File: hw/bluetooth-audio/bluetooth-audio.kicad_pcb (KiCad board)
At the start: 4 copper layers, 32.4 x 55.2 mm, 100 parts, among them J1 AudioJack4_Ground, J2 USB_C_Receptacle_USB2.0, J3 Conn_01x06, J4 2x5 JTAG header, Q1 UMH3N, U1 ESP32D0WD-V3, U2 CH340K, U3 TLV71318PDBV, U4 ES8388, U5 USBLC6-2SC6, U6 W25Q32JVZP, U7 NCP1117-3.3_SOT223, Y1 Crystal 40 MHz 10pF

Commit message: Rev B micro sheet: correctness fixes, CH340 load switch, full ESP32 GPIO map
Micro-sheet fixes (netlist-verified):
- UART TX/RX crossover corrected (U0RXD<->CH340 TXD, U0TXD<->CH340 RXD)
- Flash IO2/IO3 uncrossed (GPIO9/SPIWP->IO2, GPIO10/SPIHD->IO3)
- Digital rail unified to +3V3_SYS; EN pull-up (R11) reconnected

CH340K high-side load switch (delta #16):
- Q2 AO3401A (SOT-23, LCSC C15127) + R40 100k gate pull-down = default-ON
  so the ROM bootloader is powered for USB flashing; gate CH340_EN on GPIO21,
  firmware drives high to disable the bridge on battery

Full ESP32 interface wired (see design-overview.md 3.8):
- EN1->16, EN2->17, AUDIO_VCC_EN->4, AUDIO_SW->5, CH340_EN->21, CHARGE_EN->2
- /PGOOD->38, /CHG->32; ADC1 senses BAT_ADC->34, USB_CC1->36, USB_CC2->37,
  USB_VBUS_SENSE->39; GPIO33 spare
- AUDIO_SW drives both TS5A23159 inputs (LOW=RX, HIGH=TX); pinout verified
  against TI datasheet (COM=jack, NC=codec-out, NO=codec-in, both channels)

Docs:
- design-overview.md: committed GPIO map with strapping-pin FW/HW implications
  (3.8), AUDIO_SW/CHARGE_EN firmware notes (9), updated status (10)
- design-review-micro.md: micro-sheet systems review
- added WCH CH340 datasheet; updated TODO
- gitignore MCP snapshot/log artifacts

Co-Authored-By: Claude Opus 4.8 <noreply@anthropic.com>
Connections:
- C19 pad 1: +3V3 -> CH340_VCC
- U1 pad 42: unconnected-(U1-GPIO21-Pad42) -> CH340_EN

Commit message: Audio sheet redesign: ZTS6216 mic, PJ-3537S jack, shared 47 uF coupling
Rework the audio subsystem and record the rationale.

- Microphone: switch to ZillTek ZTS6216 (self-biased single-ended, C0G
  mic coupling C41/C42 per datasheet); pseudo-diff RIN1 provisioned DNP.
- Jack: PJ-3537S 3-pole TRS + detect switch (custom symbol + footprint).
- Coupling: single shared 47 uF electrolytic pair (C1/C21) on the jack
  side of the TX/RX switch, serving both RX and TX; R22/R23 bleed.
- TX input: BAT54S series-Schottky clamps (D7/D8) to AVDD/GND,
  line-level-only, PGA 0 dB.
- Ground loop: battery-only playback is the plan of record (no
  transformer footprint).
- Add TS5A23159 switch, ZTS6216 and PJ-3537S datasheets.
- Add systems design review (docs/design-review-audio.md) and update
  design overview with coupling-cap sizing.
- PCB layout updated to match.

Co-Authored-By: Claude Opus 4.8 <noreply@anthropic.com>
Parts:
- added C2: 1uF, Capacitor_SMD:C_1206_3216Metric, F.Cu at (188.8, 94.2)
- added C20: 1uF, Capacitor_SMD:C_0603_1608Metric, F.Cu at (207.5, 119.2)
- added C23: 1uF, Capacitor_SMD:C_0402_1005Metric, F.Cu at (218.6, 104.5)
- added C25: 1uF, Capacitor_SMD:C_0402_1005Metric, F.Cu at (218.6, 106.5)
- added C45: 10nF, Capacitor_SMD:C_0402_1005Metric, F.Cu at (218.6, 116.8)
- added C46: 100nF, Capacitor_SMD:C_0402_1005Metric, F.Cu at (218.6, 108.4)
- added C47: 10uF, Capacitor_SMD:C_1206_3216Metric, F.Cu at (188.8, 100.9)
- added C48: 47uF, Capacitor_SMD:C_1206_3216Metric, F.Cu at (188.8, 104.2)
- added C49: 47uF, Capacitor_SMD:C_1206_3216Metric, F.Cu at (188.8, 107.6)
- added C5: 10uF, Capacitor_SMD:C_1206_3216Metric, F.Cu at (188.8, 97.5)
- added C50: 10uF, Capacitor_SMD:C_1206_3216Metric, F.Cu at (188.8, 110.9)
- added C51: 4.7nF, Capacitor_SMD:C_1206_3216Metric, F.Cu at (188.8, 114.3)
- added C52: 100nF, Capacitor_SMD:C_1206_3216Metric, F.Cu at (188.8, 117.6)
- added C53: 100nF, Capacitor_SMD:C_1206_3216Metric, F.Cu at (188.8, 121.0)
- added D4: LED_3V3_AUDIO, LED_SMD:LED_0805_2012Metric, F.Cu at (208.3, 94.0)
- added D5: LED_PGOOD, LED_SMD:LED_0805_2012Metric, F.Cu at (208.3, 97.1)
- added D6: LED_CHG, LED_SMD:LED_0805_2012Metric, F.Cu at (208.3, 100.1)
- added J1: PJ-3537S-SMT, custom_footprints:PJ-3537S-SMT, F.Cu at (219.7, 98.0)
- added J2: USB_C_Receptacle_USB2.0, Connector_USB:USB_C_Receptacle_GCT_USB4110, F.Cu at (198.9, 97.8)
- added J5: Conn_01x03, Connector_Molex:Molex_Micro-Latch_53254-0370_1x03_P2.00mm_Horizontal, F.Cu at (203.4, 109.5)
- added Q2: AO3401A, Package_TO_SOT_SMD:SOT-23, F.Cu at (216.7, 113.6)
- added R15: 330R, Resistor_SMD:R_0402_1005Metric, F.Cu at (193.1, 107.5)
- added R16: 10R, Resistor_SMD:R_0402_1005Metric, F.Cu at (215.7, 97.5)
- added R17: 100k, Resistor_SMD:R_0402_1005Metric, F.Cu at (193.1, 109.5)
- added R19: 4k7, Resistor_SMD:R_0402_1005Metric, F.Cu at (215.7, 99.5)
- added R20: 4k7, Resistor_SMD:R_0402_1005Metric, F.Cu at (215.7, 101.5)
- added R21: 10R, Resistor_SMD:R_0402_1005Metric, F.Cu at (215.7, 103.4)
- added R27: 10k, Resistor_SMD:R_0402_1005Metric, F.Cu at (215.7, 105.4)
- added R28: 330R, Resistor_SMD:R_0402_1005Metric, F.Cu at (193.1, 111.4)
- added R29: 330R, Resistor_SMD:R_0402_1005Metric, F.Cu at (193.1, 113.4)
- added R30: 100k, Resistor_SMD:R_0402_1005Metric, F.Cu at (193.1, 115.4)
- added R31: 100k, Resistor_SMD:R_0402_1005Metric, F.Cu at (196.0, 103.5)
- added R32: 1k, Resistor_SMD:R_0402_1005Metric, F.Cu at (196.0, 105.5)
- added R33: 1k, Resistor_SMD:R_0402_1005Metric, F.Cu at (196.0, 107.5)
- added R34: 100k, Resistor_SMD:R_0402_1005Metric, F.Cu at (196.0, 109.5)
- added R35: 100k, Resistor_SMD:R_0402_1005Metric, F.Cu at (196.0, 111.4)
- added R36: 1k, Resistor_SMD:R_0402_1005Metric, F.Cu at (196.0, 113.4)
- added R37: 1k, Resistor_SMD:R_0402_1005Metric, F.Cu at (196.0, 115.4)
- added R38: 100k, Resistor_SMD:R_0402_1005Metric, F.Cu at (198.9, 103.5)
- added R39: 47k, Resistor_SMD:R_0402_1005Metric, F.Cu at (198.9, 105.5)
- added R4: 5k1, Resistor_SMD:R_0402_1005Metric, F.Cu at (193.1, 103.5)
- added R40: 100k, Resistor_SMD:R_0402_1005Metric, F.Cu at (215.7, 116.9)
- added R5: 5k1, Resistor_SMD:R_0402_1005Metric, F.Cu at (193.1, 105.5)
- added R7: 10R, Resistor_SMD:R_0402_1005Metric, F.Cu at (215.7, 93.5)
- added R8: 10R, Resistor_SMD:R_0402_1005Metric, F.Cu at (215.7, 95.5)
- added R_ILIM1: 1k5, Resistor_SMD:R_0402_1005Metric, F.Cu at (198.9, 107.5)
- added R_ISET1: 1k2, Resistor_SMD:R_0402_1005Metric, F.Cu at (198.9, 109.5)
- added R_ITERM1: 3k, Resistor_SMD:R_0402_1005Metric, F.Cu at (198.9, 111.4)
- added R_NTC_LIN1: 1k, Resistor_SMD:R_0402_1005Metric, F.Cu at (198.9, 113.4)
- added R_TMR1: 56k, Resistor_SMD:R_0402_1005Metric, F.Cu at (198.9, 115.4)
- added TP13: TEST_3V3_AUDIO, TestPoint:TestPoint_Pad_D1.0mm, F.Cu at (198.9, 117.9)
- added U11: LP5907MFX-3.3, Package_TO_SOT_SMD:SOT-23-5, F.Cu at (203.0, 118.9)
- added U3: TS5A23159DGS, Package_SO:TSSOP-10_3x3mm_P0.5mm, F.Cu at (223.7, 105.8)
- added U5: USBLC6-2SC6, Package_TO_SOT_SMD:SOT-23-6, F.Cu at (203.0, 114.2)
- added U7: AP7361C-33Y5, Package_TO_SOT_SMD:SOT-89-5, F.Cu at (208.9, 114.9)
- added U9: BQ24074RGT, Package_DFN_QFN:VQFN-16-1EP_3x3mm_P0.5mm_EP1.6x1.6mm, F.Cu at (194.7, 119.1)
- C3: value 10uF -> 4.7uF
- C4: value 1uF -> 4.7uF
- R12, R18, R6: value 1k -> 330R
- TP2: value TEST_3V3 -> TEST_3V3_SYS
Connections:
- net ASDOUT renamed /Micro/ASDOUT
- net DSDIN renamed /Micro/DSDIN
- net LRCK renamed /Micro/LRCK
- net MCLK renamed /Micro/GPIO_0
- net SCLK renamed /Micro/SCLK
- C10 pad 1: +3V3 -> +3V3_SYS
- C11 pad 1: +3V3 -> +3V3_SYS
- C12 pad 1: +1V8 -> +3V3_AUDIO
- C13 pad 1: +1V8 -> +3V3_AUDIO
- C14 pad 1: +1V8 -> +3V3_AUDIO
- C15 pad 1: +3V3 -> /audio/AVDD
- C16 pad 1: +3V3 -> /audio/AVDD
- C17 pad 1: +3V3 -> /audio/HPVDD
- C18 pad 1: +3V3 -> /audio/HPVDD
- C19 pad 1: CH340_VCC -> Net-(Q2-D)
- C3 pad 1: /Power/USB_VBUS -> +V_SYS
- C33 pad 1: +3V3 -> +3V3_SYS
- C4 pad 1: +3V3 -> +3V3_SYS
- C41 pad 1: Net-(MK1-OUT+) -> Net-(MK1-OUT)
- C43 pad 2: Net-(C43-Pad2) -> /audio/AVDD
- C44 pad 1: Net-(C43-Pad2) -> /audio/AVDD
- C7 pad 1: +3V3 -> +3V3_SYS
- C8 pad 1: +3V3 -> +3V3_SYS
- C9 pad 1: +3V3 -> +3V3_SYS
- J3 pad 1: +3V3 -> +3V3_SYS
- J4 pad 1: +3V3 -> +3V3_SYS
- R11 pad 2: +3V3 -> +3V3_SYS
- R24 pad 2: +3V3 -> +3V3_SYS
- R26 pad 2: +3V3 -> +3V3_SYS
- R6 pad 1: +3V3 -> +3V3_SYS
- TP14 pad 1: I2C_AD -> /audio/I2C_AD
- TP15 pad 1: I2C_CLK -> /Micro/I2C_CLK
- TP2 pad 1: +3V3 -> +3V3_SYS
- TP5 pad 1: LIN2 -> /audio/LIN2
- TP5 pad 2: RIN2 -> /audio/RIN2
- TP8 pad 1: I2C_DATA -> /Micro/I2C_DATA
- U1 pad 1: +3V3 -> +3V3_SYS
- U1 pad 10: unconnected-(U1-VDET_1/GPIO34/ADC1_CH6-Pad10) -> /Micro/BAT_ADC
- U1 pad 12: unconnected-(U1-32K_XP/GPIO32/ADC1_CH4-Pad12) -> /Micro/~{CHG}
- U1 pad 19: +3V3 -> +3V3_SYS
- U1 pad 22: /Micro/GPIO_2 -> /Micro/~{CHARGE_EN}
- U1 pad 24: unconnected-(U1-GPIO4/ADC2_CH0-Pad24) -> /Micro/AUDIO_VCC_EN
- U1 pad 25: unconnected-(U1-GPIO16-Pad25) -> /Micro/EN1
- U1 pad 27: unconnected-(U1-GPIO17-Pad27) -> /Micro/EN2
- U1 pad 3: +3V3 -> +3V3_SYS
- U1 pad 34: unconnected-(U1-GPIO5-Pad34) -> /Micro/AUDIO_SW
- U1 pad 35: I2C_CLK -> /Micro/I2C_CLK
- U1 pad 36: I2C_DATA -> /Micro/I2C_DATA
- U1 pad 37: +3V3 -> +3V3_SYS
- U1 pad 4: +3V3 -> +3V3_SYS
- U1 pad 42: CH340_EN -> /Micro/CH340_EN
- U1 pad 43: +3V3 -> +3V3_SYS
- U1 pad 46: +3V3 -> +3V3_SYS
- U1 pad 48: unconnected-(U1-CAP1-Pad48) -> Net-(U1-CAP1)
- U1 pad 5: unconnected-(U1-SENSOR_VP/GPIO36/ADC1_CH0-Pad5) -> /Micro/USB_CC1
- U1 pad 6: unconnected-(U1-SENSOR_CAPP/GPIO37/ADC1_CH1-Pad6) -> /Micro/USB_CC2
- U1 pad 7: unconnected-(U1-SENSOR_CAPN/GPIO38/ADC1_CH2-Pad7) -> /Micro/~{PGOOD}
- U1 pad 8: unconnected-(U1-SENSOR_VN/GPIO39/ADC1_CH3-Pad8) -> /Micro/USB_VBUS_SENSE
- U2 pad 1: USB_D+ -> /Micro/USB_D+
- U2 pad 10: +3V3 -> Net-(Q2-D)
- U2 pad 2: USB_D- -> /Micro/USB_D-
- U2 pad 7: +3V3 -> Net-(Q2-D)
- U2 pad 8: /Micro/UART_TX -> /Micro/UART_RX
- U2 pad 9: /Micro/UART_RX -> /Micro/UART_TX
- U4 pad 11: Net-(U4-ROUT1) -> /audio/ROUT1
- U4 pad 12: Net-(U4-LOUT1) -> /audio/LOUT1
- U4 pad 16: +3V3 -> /audio/HPVDD
- U4 pad 17: +3V3 -> /audio/AVDD
- U4 pad 2: +1V8 -> +3V3_AUDIO
- U4 pad 21: Net-(U4-RIN2) -> /audio/RIN2
- U4 pad 22: Net-(U4-LIN2) -> /audio/LIN2
- U4 pad 26: I2C_AD -> Net-(U4-CE)
- U4 pad 27: I2C_DATA -> /Micro/I2C_DATA
- U4 pad 28: I2C_CLK -> /Micro/I2C_CLK
- U4 pad 3: +1V8 -> +3V3_AUDIO
- U6 pad 3: /Micro/SWP/SD3 -> /Micro/SHD/SD2
- U6 pad 7: /Micro/SHD/SD2 -> /Micro/SWP/SD3
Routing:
- net I2C_AD: track 2.59 -> 0.00 mm
- net (no net): track 0.00 -> 2.59 mm
- added copper zone on In2.Cu, net +V_SYS
- removed copper zone on In2.Cu, net /Power/USB_VBUS

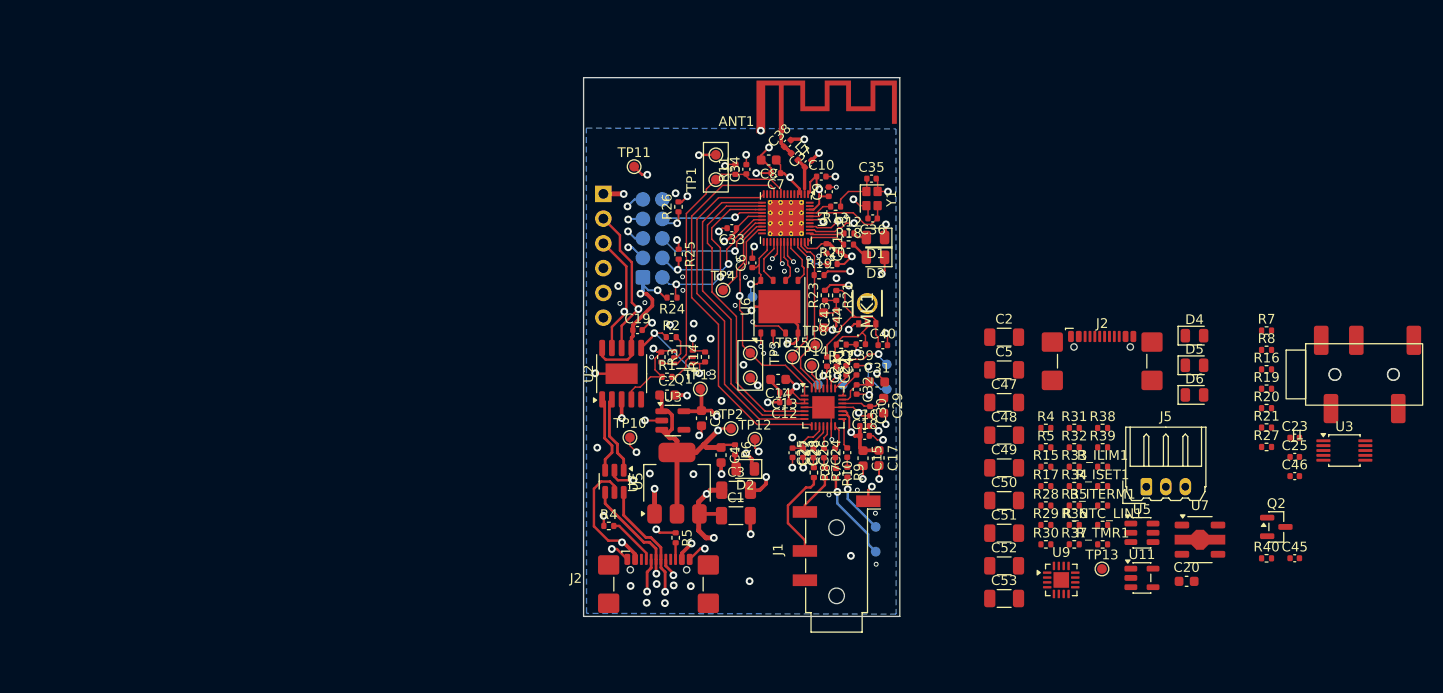
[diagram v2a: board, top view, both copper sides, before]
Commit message: Audio BOM: OUT2 couplers to electrolytic, C53 0402, C41/C42 land; place PCB
Schematic (audio + power sheets):
- C24/C26 (ES8388 OUT2 -> TP6 test-output couplers): 1uF MLCC -> 47uF
  electrolytic (Panasonic EEEFT1E470AR / C336270), matching C1/C21. Polarity
  verified against the netlist: + terminal to the codec/VMID side.
- C53 (USB_VBUS_SENSE divider filter): 1206 -> 0402 (house part
  CL05B104KO5NNNC / C1525).
- C41/C42 (mic C0G couplers): footprint aligned to plain C_1206_3216Metric,
  matching C54.

PCB: all footprints now placed in their initial positions, pending V1 routing.

Docs: design-overview.tex updated (delta #20 + 2026-09-16 revision entry). The
D7/D8 TX-input clamp removal is decided but recorded as pending -- that
schematic edit is being done by hand and is not in this commit.

Note: the deleted kicad-library submodule and the untracked in-project library
copies are deliberately left unstaged (broken/redundant state).

Co-Authored-By: Claude Opus 4.8 <noreply@anthropic.com>
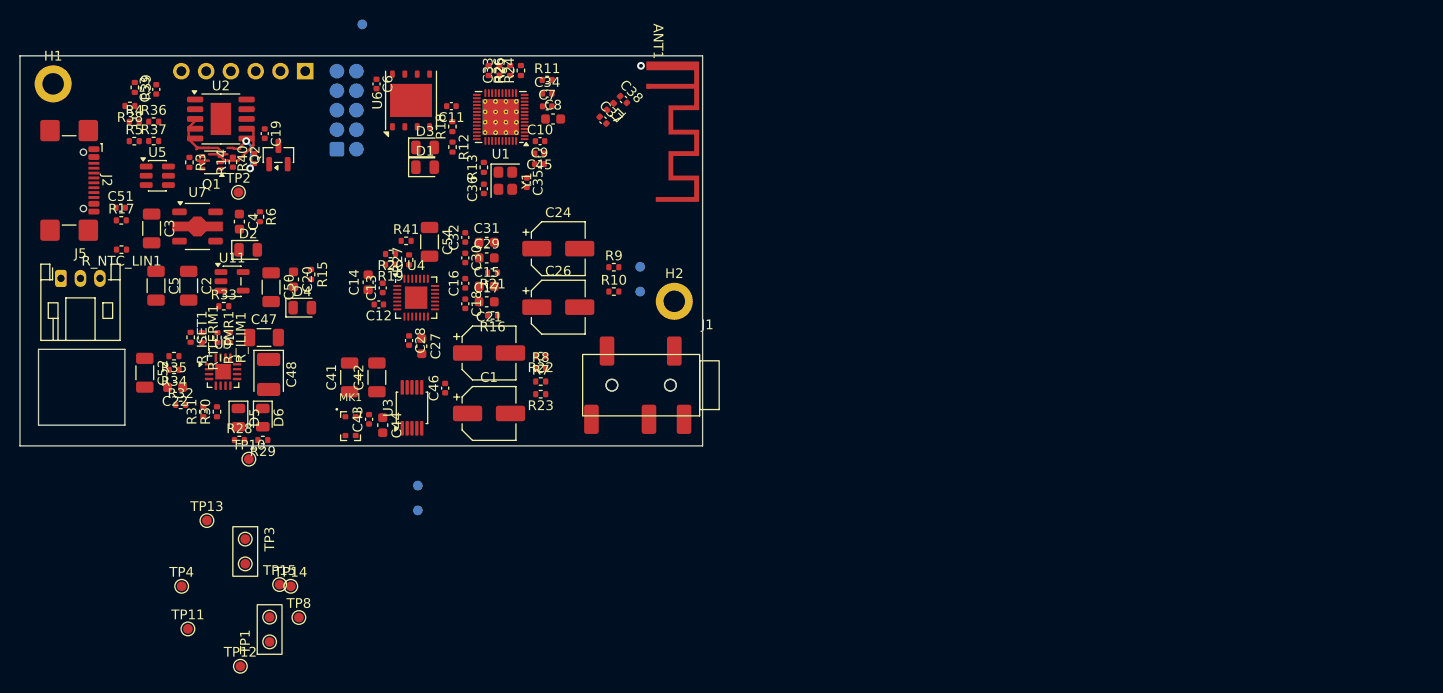
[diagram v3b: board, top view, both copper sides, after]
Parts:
- removed the C2 at (154.3, 100.1)
- removed C23 (x2), C25 (x2): 1uF, Capacitor_SMD:C_0402_1005Metric
- removed C39, C40: 10nF, Capacitor_SMD:C_0402_1005Metric
- removed C49: 47uF, Capacitor_SMD:C_1206_3216Metric
- removed the C5 at (157.8, 102.5)
- removed the J1 at (171.6, 116.0)
- removed the J2 at (153.4, 120.6)
- removed R1, R2: 10k, Resistor_SMD:R_0402_1005Metric
- removed the R19 at (169.8, 87.8)
- removed the R20 at (171.2, 86.7)
- removed the R21 at (171.6, 89.9)
- removed the R4 at (148.3, 113.5)
- removed the R5 at (155.1, 114.8)
- removed the R7 at (170.4, 108.1)
- removed the R8 at (169.3, 108.1)
- removed the TP13 at (157.7, 99.5)
- removed TP7: TEST_MIC_1, custom_footprints:TestPoint_Pad_2x1_D1.0mm
- removed the U3 at (154.9, 102.7)
- removed the U5 at (148.9, 109.0)
- removed the U7 at (155.3, 109.1)
- added C54: 100nF, Capacitor_SMD:C_1206_3216Metric, F.Cu at (129.9, 84.4)
- added H1: MountingHole, MountingHole:MountingHole_2.2mm_M2_DIN965_Pad, F.Cu at (91.3, 68.2)
- added H2: MountingHole, MountingHole:MountingHole_2.2mm_M2_DIN965_Pad, F.Cu at (155.0, 90.5)
- added R41: 0R, Resistor_SMD:R_0402_1005Metric, F.Cu at (127.5, 84.3)
- C1: value 1uF -> 47uF; footprint Capacitor_SMD:C_1206_3216Metric -> Capacitor_SMD:CP_Elec_5x5.8
- C21, C24, C26: value 1uF -> 47uF; footprint Capacitor_SMD:C_0402_1005Metric -> Capacitor_SMD:CP_Elec_5x5.8
- C22: value 1uF -> 4.7uF; footprint Capacitor_SMD:C_0402_1005Metric -> Capacitor_SMD:C_0603_1608Metric
- C27: footprint Capacitor_SMD:C_0402_1005Metric -> Capacitor_SMD:C_0603_1608Metric
- C41, C42: footprint Capacitor_SMD:C_0402_1005Metric -> Capacitor_SMD:C_1206_3216Metric
- C48: footprint Capacitor_SMD:C_1206_3216Metric -> Capacitor_Tantalum_SMD:CP_EIA-3528-21_Kemet-B
- C51, C53: footprint Capacitor_SMD:C_1206_3216Metric -> Capacitor_SMD:C_0402_1005Metric
- D1: value LED_BLUE -> LED_WHITE
- J5: footprint Connector_Molex:Molex_Micro-Latch_53254-0370_1x03_P2.00mm_Horizontal -> Connector_JST:JST_PH_S3B-PH-K_1x03_P2.00mm_Horizontal
- MK1: value ICS-40720 -> ZTS6216; footprint custom_footprints:ICS40720 -> custom_footprints:ZTS6216
- R19, R20: value 4k7 -> 1k
- R22: value 2k2 -> 100k
- R23: value 1k -> 100k
- U3: footprint Package_SO:TSSOP-10_3x3mm_P0.5mm -> Package_SO:MSOP-10_3x3mm_P0.5mm
- Y1: footprint Crystal:Crystal_SMD_SeikoEpson_FA128-4Pin_2.0x1.6mm -> Crystal:Crystal_SMD_2520-4Pin_2.5x2.0mm
- moved J5 113.3 mm to (92.1, 88.2)
- moved R40 111.6 mm to (111.9, 75.9), turned to 90 degrees
- moved Q2 109.2 mm to (114.4, 75.5), turned to 90 degrees
- moved J2 108.9 mm to (91.8, 78.1), turned to -90 degrees
- moved U7 107.7 mm to (106.1, 82.8)
- moved U5 107.4 mm to (102.0, 77.6)
- moved R39 105.9 mm to (99.7, 68.6), turned to -90 degrees
- moved R38 105.1 mm to (99.2, 70.5), turned to 180 degrees
- moved R_NTC_LIN1 104.5 mm to (98.3, 85.2), turned to 180 degrees
- moved R36 103.1 mm to (101.6, 72.1)
- moved R37 103.1 mm to (101.6, 74.1)
- moved C53 101.4 mm to (101.9, 68.8), turned to 90 degrees
- moved R17 98.7 mm to (98.3, 82.2)
- moved R4 98.6 mm to (99.6, 72.1)
- moved R5 98.6 mm to (99.6, 74.1)
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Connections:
- net /Micro/LED_BLUE renamed /Micro/LED_WHITE
- net /audio/MIC+ renamed /audio/MIC_P
- C1 pad 1: /Power/USB_VBUS -> Net-(C1-Pad1)
- C1 pad 2: GND -> Net-(C1-Pad2)
- C21 pad 1: Net-(U4-LIN2) -> Net-(C21-Pad1)
- C21 pad 2: LIN2 -> Net-(C21-Pad2)
- C22 pad 1: Net-(U4-RIN2) -> +BATT
- C22 pad 2: RIN2 -> GND
- C24 pad 1: Net-(C24-Pad1) -> Net-(U4-LOUT2)
- C24 pad 2: Net-(U4-LOUT2) -> Net-(C24-Pad2)
- C26 pad 1: Net-(C26-Pad1) -> Net-(U4-ROUT2)
- C26 pad 2: Net-(U4-ROUT2) -> Net-(C26-Pad2)
- C42 pad 1: Net-(MK1-OUT-) -> GND
- C42 pad 2: /audio/MIC- -> /audio/MIC_N
- MK1 pad 1: +3V3 -> Net-(MK1-OUT)
- MK1 pad 2: Net-(MK1-OUT-) -> GND
- MK1 pad 3: Net-(MK1-OUT+) -> GND
- MK1 pad 4: GND -> /audio/AVDD
- Q1 pad 2: Net-(Q1A-B1) -> /Micro/DTR
- Q1 pad 5: Net-(Q1B-B2) -> /Micro/RTS
- R10 pad 1: Net-(C26-Pad1) -> Net-(C26-Pad2)
- R22 pad 2: Net-(MK1-OUT-) -> Net-(C21-Pad2)
- R23 pad 1: Net-(C43-Pad2) -> GND
- R23 pad 2: +3V3 -> Net-(C1-Pad2)
- R7 pad 1: Net-(C23-Pad1) -> Net-(C1-Pad2)
- R8 pad 1: Net-(C25-Pad1) -> Net-(C21-Pad2)
- R9 pad 1: Net-(C24-Pad1) -> Net-(C24-Pad2)
- U3 pad 10: Net-(C23-Pad2) -> Net-(C1-Pad1)
- U3 pad 6: Net-(C25-Pad2) -> Net-(C21-Pad1)
- U4 pad 23: /audio/MIC- -> /audio/MIC_N_UC
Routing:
- net +3V3: track 181.8 -> 0.00 mm, vias 15 -> 0
- net GND: track 109.2 -> 0.00 mm, vias 100 -> 1
- net /Micro/UART_RX: track 45.0 -> 0.00 mm, vias 2 -> 0
- net /Micro/UART_TX: track 42.9 -> 0.00 mm, vias 2 -> 0
- net /Micro/ASDOUT: track 40.3 -> 0.00 mm
- net /Micro/LRCK: track 35.7 -> 0.00 mm
- net /Micro/DSDIN: track 33.6 -> 0.00 mm
- net /Micro/SCLK: track 32.0 -> 0.00 mm
- net /Micro/EN: track 30.2 -> 0.00 mm
- net /Micro/GPIO_0: track 31.5 -> 5.45 mm
- net /Power/USB_VBUS: track 25.6 -> 0.00 mm, vias 4 -> 0
- net +1V8: track 22.8 -> 0.00 mm, vias 2 -> 0
- net I2C_CLK: track 19.1 -> 0.00 mm, vias 2 -> 0
- net /Micro/MTMS: track 19.1 -> 0.00 mm, vias 2 -> 0
- net Net-(J2-D--PadA7): track 17.6 -> 0.00 mm, vias 2 -> 0
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- removed copper zone on In2.Cu, net +V_SYS
- removed copper zone on B.Cu, net GND
- removed copper zone on In1.Cu, net GND
- removed copper zone on In2.Cu, net GND
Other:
- board size 32.4 x 55.2 mm -> 70 x 40 mm

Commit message: PCB: 4-layer SIG-GND-PWR/GND-SIG stackup
In1.Cu is a solid GND plane; In2.Cu carries the +3V3_SYS pour with GND
fill, so both outer signal layers sit over an adjacent uninterrupted
reference plane. Board setup (design rules, via sizes, netclasses) and
the JLCPCB custom DRU updated alongside the layout.

Co-Authored-By: Claude Opus 5.5 <noreply@anthropic.com>
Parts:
- removed TP14: TEST_I2C_AD, TestPoint:TestPoint_Pad_D1.0mm
- added C23: 100nF, Capacitor_SMD:C_0402_1005Metric, F.Cu at (136.0, 76.0)
- TP6: moved to F.Cu
- moved TP1 66.5 mm to (144.3, 66.5), turned to 0 degrees
- moved TP12 60.4 mm to (146.1, 79.2)
- moved TP4 59.9 mm to (146.0, 76.6)
- moved TP3 49.6 mm to (98.6, 66.9), turned to 180 degrees
- moved TP8 46.2 mm to (126.6, 77.9)
- moved TP15 41.4 mm to (125.1, 79.5)
- moved TP13 29.4 mm to (115.9, 84.9)
- moved TP11 21.7 mm to (100.9, 102.8)
- moved R_NTC_LIN1 10.0 mm to (103.0, 94.0), turned to -90 degrees
- moved TP5 8.38 mm to (125.4, 101.7)
- moved TP10 7.05 mm to (104.7, 104.4)
- moved R18 6.04 mm to (130.3, 78.3), turned to -90 degrees
- moved TP6 5.06 mm to (156.4, 85.9)
- moved C42 4.73 mm to (119.8, 98.8)
- moved R25 4.72 mm to (131.2, 66.8), turned to 0 degrees
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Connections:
- net Net-(ANT1-IN) renamed /Micro/ANT_FEED
- net Net-(J2-D+-PadA6) renamed /Power/USB_CONN_D+
- net Net-(J2-D--PadA7) renamed /Power/USB_CONN_D-
- net Net-(U1-LNA_IN) renamed /Micro/LNA_IN
- U1 pad 10: /Micro/BAT_ADC -> /Micro/USB_VBUS_SENSE
- U1 pad 22: /Micro/~{CHARGE_EN} -> /Micro/AUDIO_VCC_EN
- U1 pad 24: /Micro/AUDIO_VCC_EN -> /Micro/~{CHARGE_EN}
- U1 pad 25: /Micro/EN1 -> /Micro/EN2
- U1 pad 27: /Micro/EN2 -> /Micro/EN1
- U1 pad 5: /Micro/USB_CC1 -> /Micro/USB_CC2
- U1 pad 6: /Micro/USB_CC2 -> /Micro/USB_CC1
- U1 pad 8: /Micro/USB_VBUS_SENSE -> /Micro/BAT_ADC
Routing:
- net +3V3_SYS: track 0.00 -> 164.2 mm, vias 0 -> 10
- net GND: track 0.00 -> 132.4 mm, vias 1 -> 96
- net /Micro/BAT_ADC: track 0.00 -> 84.7 mm, vias 0 -> 2
- net /Micro/GPIO_0: track 5.45 -> 76.6 mm, vias 2 -> 4
- net /Micro/~{CHG}: track 0.00 -> 71.0 mm, vias 0 -> 2
- net /Micro/~{PGOOD}: track 0.00 -> 66.3 mm, vias 0 -> 2
- net /Micro/~{CHARGE_EN}: track 0.00 -> 61.1 mm, vias 0 -> 3
- net /Micro/EN2: track 0.00 -> 60.1 mm, vias 0 -> 2
- net /Micro/USB_VBUS_SENSE: track 0.00 -> 59.0 mm, vias 0 -> 2
- net /Micro/EN1: track 0.00 -> 58.9 mm, vias 0 -> 2
- net +3V3_AUDIO: track 0.00 -> 57.0 mm, vias 0 -> 5
- net +V_SYS: track 0.00 -> 56.5 mm, vias 0 -> 4
- net /Micro/AUDIO_SW: track 0.00 -> 54.2 mm, vias 0 -> 2
- net /Micro/USB_CC2: track 0.00 -> 51.7 mm, vias 0 -> 2
- net /Micro/EN: track 0.00 -> 51.1 mm, vias 0 -> 2
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- added copper zone on In2.Cu, net +3V3_SYS
- added copper zone on In1.Cu, net GND
- added copper zone on In2.Cu, net GND
